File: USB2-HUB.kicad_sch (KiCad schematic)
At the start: 40 parts, among them J4 USB_OTG, U2 TLV71311PDBV, U3 FSUSB42MUX, U5 TPD4EUSB30, U6 TUSB4041I, Y1 24.000MHz XTAL

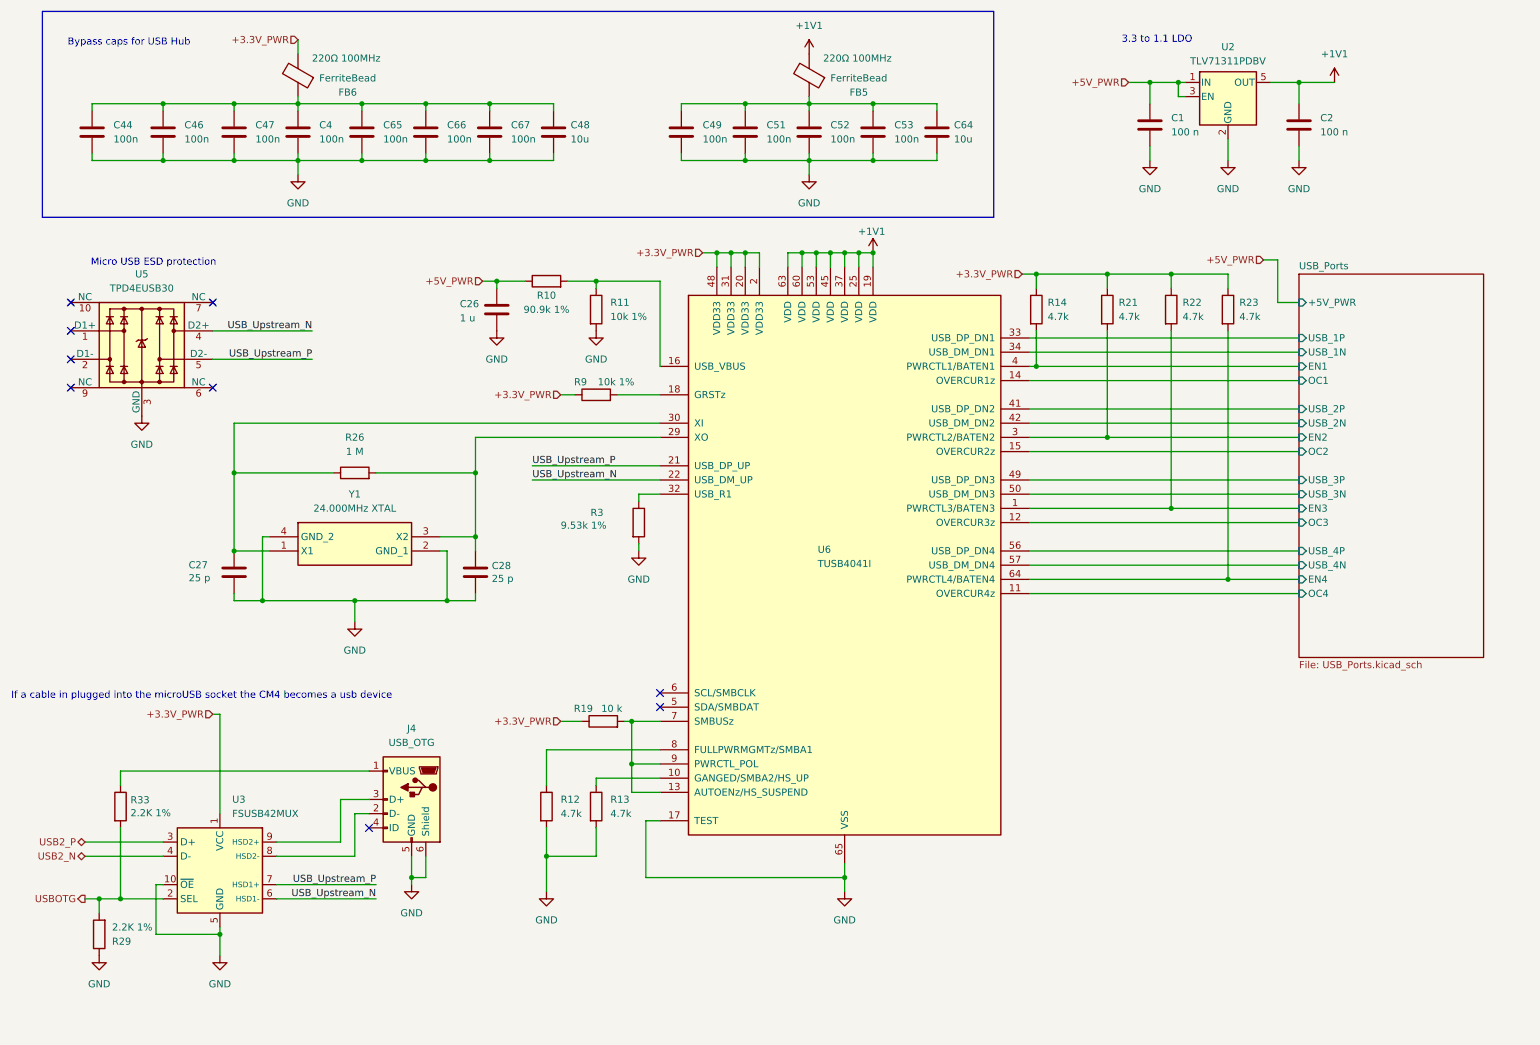
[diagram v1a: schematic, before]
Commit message: added parts to almost everything (except can xtal and fuses)
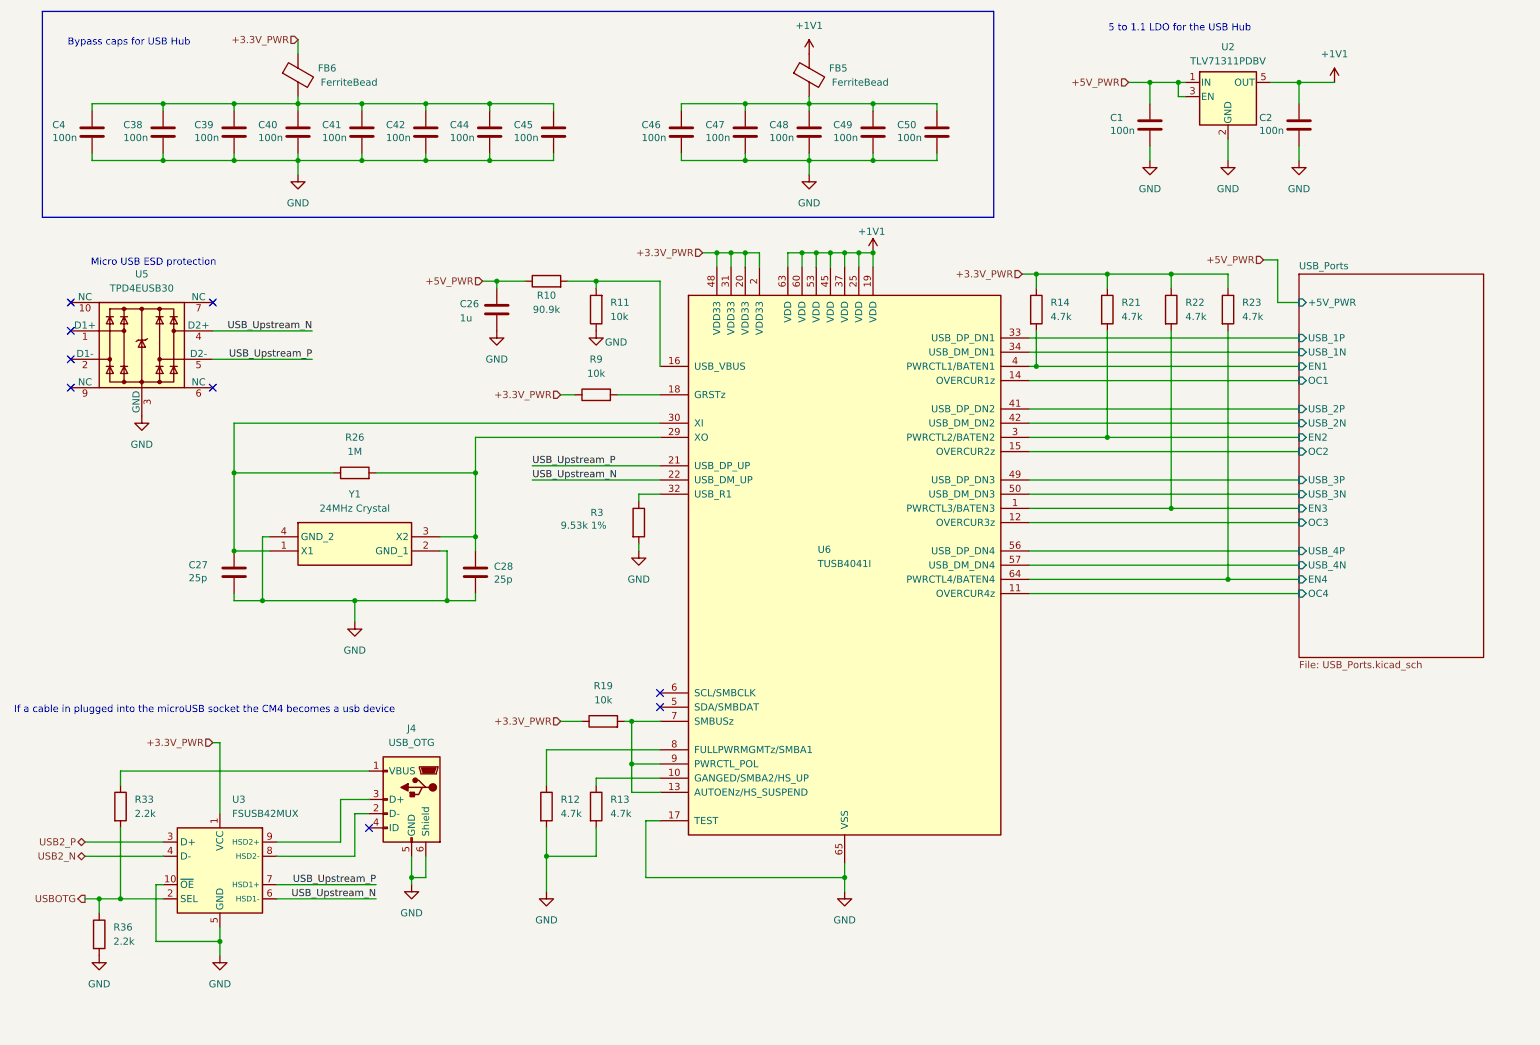
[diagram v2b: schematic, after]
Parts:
- removed C51, C52, C53, C65, C66, C67: 100n, symbol Device:C
- removed C64: 10u, symbol Device:C
- removed R29: 2.2K 1%, Resistor_SMD:R_0402_1005Metric, symbol Device:R
- added C38, C39, C40, C41, C42, C45, C50: 100n, Capacitor_SMD:C_0805_2012Metric, symbol Device:C
- added R36: 2.2k, Resistor_SMD:R_0402_1005Metric, symbol Device:R
- C1, C2: value 100 n -> 100n; footprint (none) -> Capacitor_SMD:C_0805_2012Metric; P/N (none) -> C0805C104M5RACTU
- C26: value 1 u -> 1u; footprint (none) -> Capacitor_SMD:C_0805_2012Metric; P/N (none) -> C0805C105K5PACTU
- C27, C28: value 25 p -> 25p; footprint Capacitor_SMD:C_0402_1005Metric -> Capacitor_SMD:C_0603_1608Metric; Field4 Digikey -> (none); Field5 490-17672-1-ND -> (none); Field6 GJM1555C1H270JB01D -> (none); Field7 Murata -> (none); Field8 UCAP00738 -> (none); P/N (none) -> CC0603JRNPO9BN250; Part Description 27pF 5% 50V Ceramic Capacitor C0G, NP0 0402 (1005 Metric) -> (none)
- C4, C44, C46, C47, C49: footprint (none) -> Capacitor_SMD:C_0805_2012Metric; P/N (none) -> C0805C104M5RACTU
- C48: value 10u -> 100n; footprint (none) -> Capacitor_SMD:C_0805_2012Metric; P/N (none) -> C0805C104M5RACTU
- FB5, FB6: footprint (none) -> Inductor_SMD:L_1206_3216Metric; P/N (none) -> BMC-Q2CY0220H; Part # BMC-Q2CY0220H -> (none); Spec 220Ω 100MHz -> (none)
- J4: footprint (none) -> Connector_USB:USB_Micro-B_Molex-105017-0001; P/N (none) -> 105017-0001
- R10: value 90.9k 1% -> 90.9k; footprint (none) -> Resistor_SMD:R_1206_3216Metric; P/N (none) -> CRCW120690K9FKEA
- R11, R9: value 10k 1% -> 10k; footprint (none) -> Resistor_SMD:R_0805_2012Metric; P/N (none) -> CRCW080510K0FKEAC
- R12, R13, R14, R21, R22, R23: footprint (none) -> Resistor_SMD:R_0805_2012Metric; P/N (none) -> CRCW08054K70FKEAC
- R19: value 10 k -> 10k; footprint (none) -> Resistor_SMD:R_0805_2012Metric; P/N (none) -> CRCW080510K0FKEAC
- R26: value 1 M -> 1M; footprint (none) -> Resistor_SMD:R_0805_2012Metric; P/N (none) -> CRCW08051M00FKEA
- R33: value 2.2K 1% -> 2.2k; Field4 Farnell -> (none); Field5 9239278 -> (none); Field6 RK73G1ETQTP2201D -> (none); Field7 KOA EUROPE GMBH -> (none); Field8 120889581 -> (none); P/N (none) -> 2019-RK73G1ETTP2201DTR-ND; Part Description Resistor 2.2K M1005 1% 63mW -> (none)
- U2: P/N (none) -> TLV71311PDBV
- U3: P/N (none) -> FSUSB42MUX
- U5: P/N (none) -> TPD4EUSB30
- Y1: value 24.000MHz XTAL -> 24MHz Crystal; footprint ABM8AIG25000MHZ122ZT3 -> Controls_Pi:ABM8AIG25000MHZ122ZT3; Height 0.8 -> (none); Manufacturer_Name ABRACON -> (none); Manufacturer_Part_Number ABM8AIG-24.000MHZ-12-2Z-T3 -> (none); Mouser Part Number 815-M8AIG-24-12-2ZT3 -> (none); Mouser Price/Stock https://www.mouser.co.uk/ProductDetail/ABRACON/ABM8AIG-2400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 -> (none); P/N (none) -> ABM8AIG-24.000MHZ-12-2Z-T3
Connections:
- net +1V1: now also FB5.1; no longer FB5.2
- net +3.3V_PWR: now also FB6.1; no longer FB6.2
- net GND: now also R11.1, C38.2, C39.2, C40.2, C41.2, C42.2, C45.2, C50.2, R36.2; no longer R11.2
- net USBOTG: now also R36.1
- net at C46.1, C47.1, C48.1: now also C49.1, FB5.2, C50.1; no longer C4.1, C44.1, FB6.1
- net at R10.2, U6.16 (USB_VBUS): now also R11.2; no longer R11.1
- new net: C38.1, C39.1, C4.1, C40.1, C41.1, C42.1, C44.1, C45.1, FB6.2
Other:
- note added: "5 to 1.1 LDO for the USB Hub"
- note removed: "3.3 to 1.1 LDO"

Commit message: fixed cap sizes, added remaining parts, fixed rtc battery
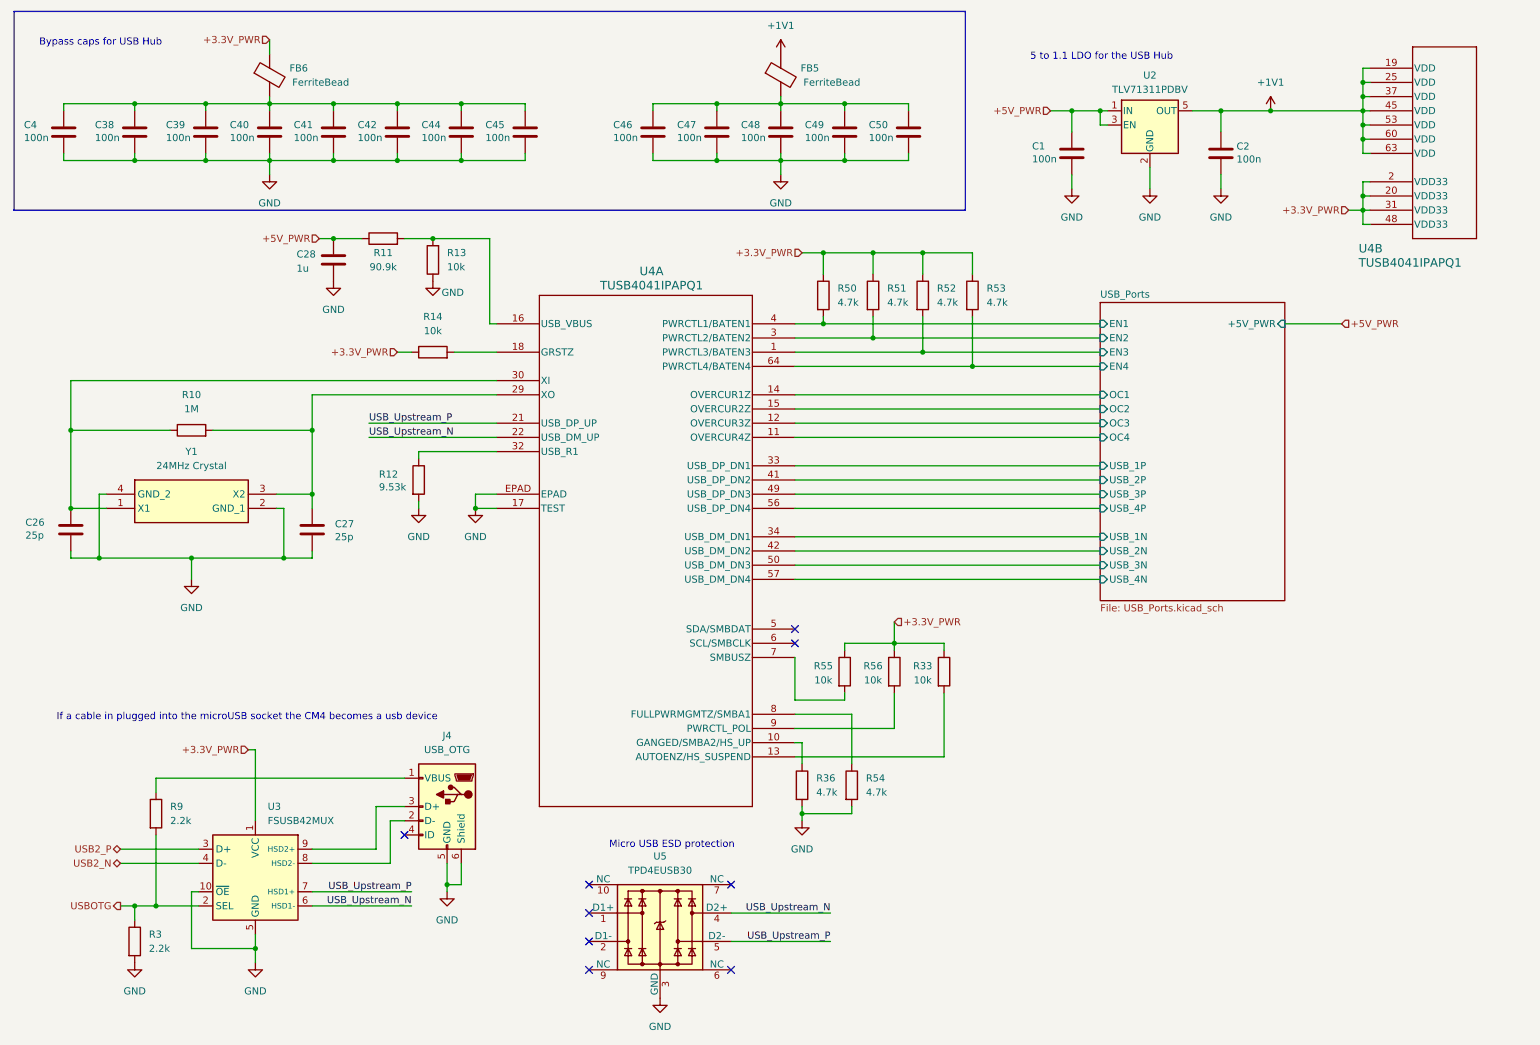
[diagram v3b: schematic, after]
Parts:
- removed R19: 10k, Resistor_SMD:R_0805_2012Metric, symbol Device:R
- removed R21, R22, R23: 4.7k, Resistor_SMD:R_0805_2012Metric, symbol Device:R
- removed R26: 1M, Resistor_SMD:R_0805_2012Metric, symbol Device:R
- removed U6: TUSB4041I, Package_QFP:HTQFP-64-1EP_10x10mm_P0.5mm_EP8x8mm_Mask4.4x4.4mm_ThermalVias, symbol Interface_USB:TUSB4041I
- added R50, R51, R52, R53, R54: 4.7k, Resistor_SMD:R_0805_2012Metric, symbol Device:R
- added R55, R56: 10k, Resistor_SMD:R_0805_2012Metric, symbol Device:R
- added U4: TUSB4041IPAPQ1, Controls_Pi:PAP64_4P15X4P15_TEX, symbol TUSB4041I-Q1:TUSB4041IPAPQ1
- C26: value 1u -> 25p; P/N C0805C105K5PACTU -> CC0805JRNPO9BN250
- C27: footprint Capacitor_SMD:C_0603_1608Metric -> Capacitor_SMD:C_0805_2012Metric; P/N CC0603JRNPO9BN250 -> CC0805JRNPO9BN250
- C28: value 25p -> 1u; footprint Capacitor_SMD:C_0603_1608Metric -> Capacitor_SMD:C_0805_2012Metric; P/N CC0603JRNPO9BN250 -> C0805C105K5PACTU
- R10: value 90.9k -> 1M; footprint Resistor_SMD:R_1206_3216Metric -> Resistor_SMD:R_0805_2012Metric; P/N CRCW120690K9FKEA -> CRCW08051M00FKEA
- R11: value 10k -> 90.9k; P/N CRCW080510K0FKEAC -> CRCW080590K9FKEA
- R12: value 4.7k -> 9.53k; P/N CRCW08054K70FKEAC -> RC0805FR-079K53L
- R13, R14: value 4.7k -> 10k; P/N CRCW08054K70FKEAC -> CRCW080510K0FKEAC
- R3: value 9.53k 1% -> 2.2k; footprint (none) -> Resistor_SMD:R_0805_2012Metric; P/N (none) -> RC0805FR-132K2L
- R33: value 2.2k -> 10k; footprint Resistor_SMD:R_0402_1005Metric -> Resistor_SMD:R_0805_2012Metric; P/N 2019-RK73G1ETTP2201DTR-ND -> CRCW080510K0FKEAC
- R36: value 2.2k -> 4.7k; footprint Resistor_SMD:R_0402_1005Metric -> Resistor_SMD:R_0805_2012Metric; P/N 2019-RK73G1ETTP2201DTR-ND -> CRCW08054K70FKEAC
- R9: value 10k -> 2.2k; P/N CRCW080510K0FKEAC -> RC0805FR-132K2L
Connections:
- net +1V1: now also U4.19 (VDD), U4.25 (VDD), U4.37 (VDD), U4.45 (VDD), U4.53 (VDD), U4.60 (VDD), U4.63 (VDD)
- net +3.3V_PWR: now also R33.1, R50.1, R51.1, R52.1, R53.1, R55.1, R56.1, U4.2 (VDD33), U4.20 (VDD33), U4.31 (VDD33), U4.48 (VDD33); no longer R9.1
- net +5V_PWR: now also C28.1, R11.1; no longer C26.1, R10.1
- net GND: now also R13.1, R54.2, U4.17 (TEST), U4.EPAD; no longer R11.1, R13.2
- net USBOTG: now also R3.1, R9.2; no longer R33.2, R36.1
- net USB_Ports/EN1: now also R50.2, U4.4 (PWRCTL1/BATEN1); no longer R14.2
- net USB_Ports/EN2: now also R51.2, U4.3 (PWRCTL2/BATEN2)
- net USB_Ports/EN3: now also R52.2, U4.1 (PWRCTL3/BATEN3)
- net USB_Ports/EN4: now also R53.2, U4.64 (PWRCTL4/BATEN4)
- net USB_Ports/OC1: now also U4.14 (OVERCUR1Z)
- net USB_Ports/OC2: now also U4.15 (OVERCUR2Z)
- net USB_Ports/OC3: now also U4.12 (OVERCUR3Z)
- net USB_Ports/OC4: now also U4.11 (OVERCUR4Z)
- net USB_Ports/USB_1N: now also U4.34 (USB_DM_DN1)
- net USB_Ports/USB_1P: now also U4.33 (USB_DP_DN1)
- net USB_Ports/USB_2N: now also U4.42 (USB_DM_DN2)
- net USB_Ports/USB_2P: now also U4.41 (USB_DP_DN2)
- net USB_Ports/USB_3N: now also U4.50 (USB_DM_DN3)
- net USB_Ports/USB_3P: now also U4.49 (USB_DP_DN3)
- net USB_Ports/USB_4N: now also U4.57 (USB_DM_DN4)
- net USB_Ports/USB_4P: now also U4.56 (USB_DP_DN4)
- net USB_Upstream_N: now also U4.22 (USB_DM_UP)
- net USB_Upstream_P: now also U4.21 (USB_DP_UP)
- net at J4.1 (VBUS): now also R9.1; no longer R33.1
- net at R12.1: now also U4.32 (USB_R1)
- net at R10.2: now also C27.1, Y1.3 (X2), U4.29 (XO); no longer R11.2
- net at Y1.1 (X1): now also C26.1, R10.1, U4.30 (XI); no longer C27.1
- new net: R55.2, U4.7 (SMBUSZ)
- new net: R56.2, U4.9 (PWRCTL_POL)
- new net: R33.2, U4.13 (AUTOENZ/HS_SUSPEND)
- new net: R14.2, U4.18 (GRSTZ)
- new net: R54.1, U4.8 (FULLPWRMGMTZ/SMBA1)
- new net: R36.1, U4.10 (GANGED/SMBA2/HS_UP)
- new net: R11.2, R13.2, U4.16 (USB_VBUS)
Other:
- moved on the sheet: C1, C2, C38, C39, C4, C40, C41, C42, C44, C45, C46, C47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

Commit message: review committee changes implmented
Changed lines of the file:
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@@
-			)
-		)
-		(pin "USB_2P" input
-			(at 208.28 97.79 180)
-			(effects
-				(font
-					(size 1.27 1.27)
-				)
-				(justify left)
-			)
-		)
-		(pin "USB_2N" input
-			(at 208.28 110.49 180)
-			(effects
-				(font
-					(size 1.27 1.27)
-				)
-				(justify left)
-			)
-		)
-		(pin "USB_1N" input
-			(at 208.28 107.95 180)
-			(effects
-				(font
-					(size 1.27 1.27)
-				)
-				(justify left)
-			)
-		)
-		(pin "USB_1P" input
-			(at 208.28 95.25 180)
-			(effects
-				(font
-					(size 1.27 1.27)
-				)
-				(justify left)
-			)
-		)
-		(pin "USB_4P" input
-			(at 208.28 102.87 180)
-			(effects
-				(font
-					(size 1.27 1.27)
-				)
-				(justify left)
-			)
-		)
-		(pin "USB_4N" input
-			(at 208.28 115.57 180)
-			(effects
-				(font
-					(size 1.27 1.27)
-				)
-				(justify left)
-			)
-		)
-		(pin "USB_3N" input
-			(at 208.28 113.03 180)
-			(effects
-				(font
-					(size 1.27 1.27)
-				)
-				(justify left)
-			)
-		)
-		(pin "OC1" input
-			(at 208.28 82.55 180)
-			(effects
-				(font
-					(size 1.27 1.27)
-				)
-				(justify left)
 			)
 		)
 		(pin "EN1" input
 			(at 208.28 69.85 180)
-			(effects
-				(font
-					(size 1.27 1.27)
-				)
-				(justify left)
-			)
-		)
-		(pin "OC2" input
-			(at 208.28 85.09 180)
 			(effects
 				(font
@@
 			)
 		)
-		(pin "OC3" input
+		(pin "USB_4N" bidirectional
+			(at 208.28 115.57 180)
+			(effects
+				(font
+					(size 1.27 1.27)
+				)
+				(justify left)
+			)
+		)
+		(pin "OC4" output
+			(at 208.28 90.17 180)
+			(effects
+				(font
+					(size 1.27 1.27)
+				)
+				(justify left)
+			)
+		)
+		(pin "OC3" output
 			(at 208.28 87.63 180)
 			(effects
@@
 			)
 		)
-		(pin "OC4" input
-			(at 208.28 90.17 180)
+		(pin "OC2" output
+			(at 208.28 85.09 180)
 			(effects
 				(font
@@
 			)
 		)
-		(pin "USB_3P" input
+		(pin "OC1" output
+			(at 208.28 82.55 180)
+			(effects
+				(font
+					(size 1.27 1.27)
+				)
+				(justify left)
+			)
+		)
+		(pin "USB_4P" bidirectional
+			(at 208.28 102.87 180)
+			(effects
+				(font
+					(size 1.27 1.27)
+				)
+				(justify left)
+			)
+		)
+		(pin "USB_2P" bidirectional
+			(at 208.28 97.79 180)
+			(effects
+				(font
+					(size 1.27 1.27)
+				)
+				(justify left)
+			)
+		)
+		(pin "USB_2N" bidirectional
+			(at 208.28 110.49 180)
+			(effects
+				(font
+					(size 1.27 1.27)
+				)
+				(justify left)
+			)
+		)
+		(pin "USB_1P" bidirectional
+			(at 208.28 95.25 180)
+			(effects
+				(font
+					(size 1.27 1.27)
+				)
+				(justify left)
+			)
+		)
+		(pin "USB_3P" bidirectional
 			(at 208.28 100.33 180)
 			(effects
 				(font
+					(size 1.27 1.27)
+				)
+				(justify left)
+			)
+		)
+		(pin "USB_3N" bidirectional
+			(at 208.28 113.03 180)
+			(effects
+				(font
+					(size 1.27 1.27)
+				)
+				(justify left)
+			)
+		)
+		(pin "USB_1N" bidirectional
+			(at 208.28 107.95 180)
+			(effects
+				(font
